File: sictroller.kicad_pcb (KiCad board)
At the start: 6 copper layers, 314 parts, among them J1 CONN_01X02, J10 CONN_01X02, J11 RINGTERM, J12 RINGTERM, J13 CONN_01X01, J2 CONN_01X08, J3 CONN_02X05, J4 RINGTERM, J5 RINGTERM, J6 RINGTERM, J7 CONN_01X02, J8 RINGTERM, J9 RINGTERM, P1 CONN_01X03, Q1 CSD17483F4, Q2 CCS050M12CM2, T1 7508110151, U1 ACPL-M61L, U10 74LVC2G04, U11 TXS0108E, U12 MGJ1, U13 MGJ1, U14 2ED020I12-F2, U15 MGJ1, U16 MGJ1, U17 2ED020I12-F2, U18 MGJ1, U19 MGJ1, U2 TMS320F28069M, U20 2ED020I12-F2, U3 ADM3053, U4 TPS76201, U5 TPS76201, U6 XCL221B18, U7 VIPER26HD, U8 ADUM5241, U9 MAX6691, Y1 CSTCE20M0V13C

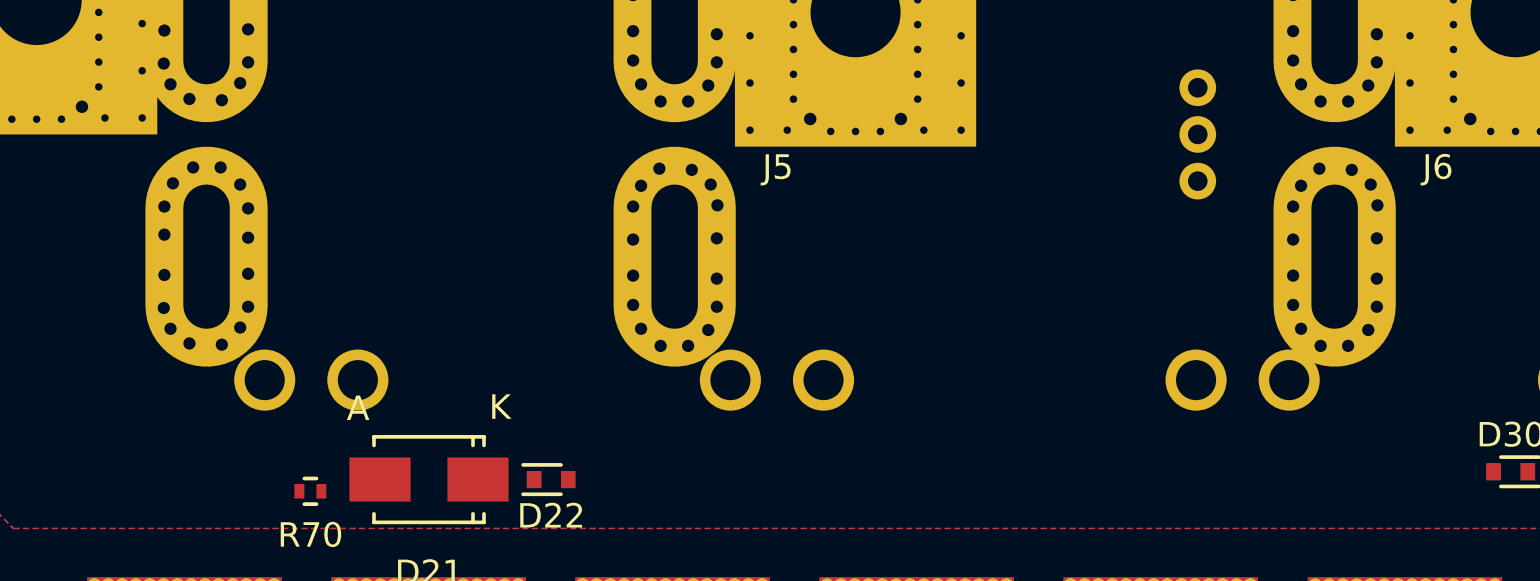
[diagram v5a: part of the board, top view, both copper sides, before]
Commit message: Zones for phase connections
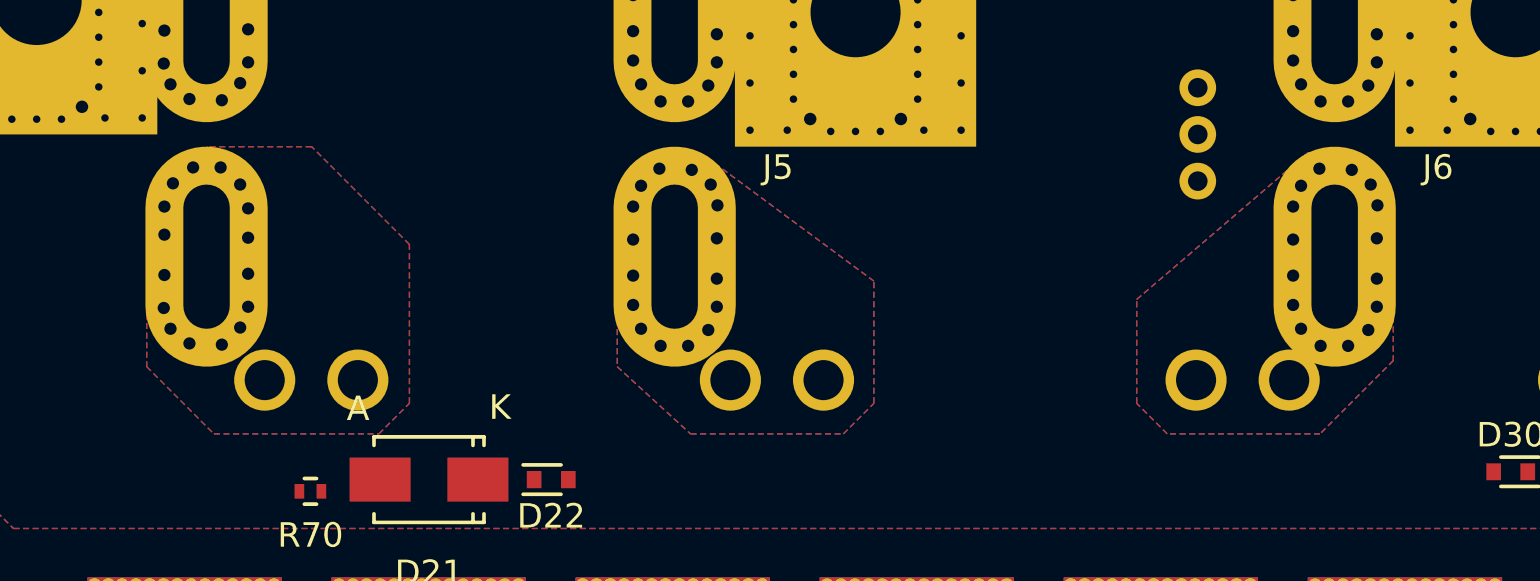
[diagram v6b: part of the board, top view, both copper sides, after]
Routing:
- added copper zone on B.Cu, net PHASE_A
- added copper zone on F.Cu, net PHASE_A
- added copper zone on In1.Cu, net PHASE_A
- added copper zone on In2.Cu, net PHASE_A
- added copper zone on In3.Cu, net PHASE_A
- added copper zone on In4.Cu, net PHASE_A
- added copper zone on B.Cu, net PHASE_B
- added copper zone on F.Cu, net PHASE_B
- added copper zone on In1.Cu, net PHASE_B
- added copper zone on In2.Cu, net PHASE_B
- added copper zone on In3.Cu, net PHASE_B
- added copper zone on In4.Cu, net PHASE_B
- added copper zone on B.Cu, net PHASE_C
- added copper zone on F.Cu, net PHASE_C
- added copper zone on In1.Cu, net PHASE_C
- added copper zone on In2.Cu, net PHASE_C
- added copper zone on In3.Cu, net PHASE_C
- added copper zone on In4.Cu, net PHASE_C
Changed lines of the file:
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@@
 (kicad_pcb (version 4) (host pcbnew 4.0.4+dfsg1-stable)
   (general
-    (links 0)
-    (no_connects 664)
+    (links 2688)
+    (no_connects 658)
     (area 0 0 0 0)
     (thickness 2.36)
@@
   (layers
     (0 F.Cu signal)
-    (1 In1.Cu mixed hide)
-    (2 In2.Cu mixed hide)
-    (3 In3.Cu mixed hide)
-    (4 In4.Cu mixed hide)
+    (1 In1.Cu mixed)
+    (2 In2.Cu mixed)
+    (3 In3.Cu mixed)
+    (4 In4.Cu mixed)
     (31 B.Cu signal)
     (32 B.Adhes user hide)
@@
     (trace_clearance 0.177)
     (zone_clearance 0.4)
-    (zone_45_only yes)
+    (zone_45_only no)
     (trace_min 0.177)
     (segment_width 0.2)
@@
       )
     )
+  )
+  (zone (net 58) (net_name PHASE_A) (layer F.Cu) (hatch edge 0.508)
+    (connect_pads yes (clearance 0.8))
+    (min_thickness 0.2032)
+    (fill yes (arc_segments 32) (thermal_gap 0.508) (thermal_bridge_width 0.508))
+    (polygon
+      (pts
+        (xy 84.5 51.25) (xy 85.75 50) (xy 85.75 43.5) (xy 81.75 39.5) (xy 77.5 39.5)
+        (xy 75 42) (xy 75 48.5) (xy 77.75 51.25)
+      )
+    )
+  )
+  (zone (net 65) (net_name PHASE_B) (layer F.Cu) (hatch edge 0.508)
+    (connect_pads yes (clearance 0.8))
+    (min_thickness 0.2032)
+    (fill yes (arc_segments 32) (thermal_gap 0.508) (thermal_bridge_width 0.508))
+    (polygon
+      (pts
+        (xy 103.5 51.25) (xy 104.75 50) (xy 104.75 45) (xy 98 40) (xy 95.25 40)
+        (xy 94.25 42.25) (xy 94.25 48.5) (xy 97.25 51.25)
+      )
+    )
+  )
+  (zone (net 72) (net_name PHASE_C) (layer F.Cu) (hatch edge 0.508)
+    (connect_pads yes (clearance 0.8))
+    (min_thickness 0.2032)
+    (fill yes (arc_segments 32) (thermal_gap 0.508) (thermal_bridge_width 0.508))
+    (polygon
+      (pts
+        (xy 116.75 51.25) (xy 115.5 50) (xy 115.5 45.75) (xy 122.5 39.75) (xy 124.5 39.75)
+        (xy 126 41.75) (xy 126 48.25) (xy 123 51.25)
+      )
+    )
+  )
+  (zone (net 58) (net_name PHASE_A) (layer B.Cu) (hatch edge 0.508)
+    (connect_pads yes (clearance 0.8))
+    (min_thickness 0.2032)
+    (fill yes (arc_segments 32) (thermal_gap 0.508) (thermal_bridge_width 0.508))
+    (polygon
+      (pts
+        (xy 84.5 51.25) (xy 85.75 50) (xy 85.75 43.5) (xy 81.75 39.5) (xy 77.5 39.5)
+        (xy 75 42) (xy 75 48.5) (xy 77.75 51.25)
+      )
+    )
+  )
+  (zone (net 58) (net_name PHASE_A) (layer In1.Cu) (hatch edge 0.508)
+    (connect_pads yes (clearance 0.4))
+    (min_thickness 0.2032)
+    (fill yes (arc_segments 32) (thermal_gap 0.508) (thermal_bridge_width 0.508))
+    (polygon
+      (pts
+        (xy 84.5 51.25) (xy 85.75 50) (xy 85.75 43.5) (xy 81.75 39.5) (xy 77.5 39.5)
+        (xy 75 42) (xy 75 48.5) (xy 77.75 51.25)
+      )
+    )
+  )
+  (zone (net 58) (net_name PHASE_A) (layer In2.Cu) (hatch edge 0.508)
+    (connect_pads yes (clearance 0.4))
+    (min_thickness 0.2032)
+    (fill yes (arc_segments 32) (thermal_gap 0.508) (thermal_bridge_width 0.508))
+    (polygon
+      (pts
+        (xy 84.5 51.25) (xy 85.75 50) (xy 85.75 43.5) (xy 81.75 39.5) (xy 77.5 39.5)
+        (xy 75 42) (xy 75 48.5) (xy 77.75 51.25)
+      )
+    )
+  )
+  (zone (net 58) (net_name PHASE_A) (layer In3.Cu) (hatch edge 0.508)
+    (connect_pads yes (clearance 0.4))
+    (min_thickness 0.2032)
+    (fill yes (arc_segments 32) (thermal_gap 0.508) (thermal_bridge_width 0.508))
+    (polygon
+      (pts
+        (xy 84.5 51.25) (xy 85.75 50) (xy 85.75 43.5) (xy 81.75 39.5) (xy 77.5 39.5)
+        (xy 75 42) (xy 75 48.5) (xy 77.75 51.25)
+      )
+    )
+  )
+  (zone (net 58) (net_name PHASE_A) (layer In4.Cu) (hatch edge 0.508)
+    (connect_pads yes (clearance 0.4))
+    (min_thickness 0.2032)
+    (fill yes (arc_segments 32) (thermal_gap 0.508) (thermal_bridge_width 0.508))
+    (polygon
+      (pts
+        (xy 84.5 51.25) (xy 85.75 50) (xy 85.75 43.5) (xy 81.75 39.5) (xy 77.5 39.5)
+        (xy 75 42) (xy 75 48.5) (xy 77.75 51.25)
+      )
+    )
+  )
+  (zone (net 65) (net_name PHASE_B) (layer B.Cu) (hatch edge 0.508)
+    (connect_pads yes (clearance 0.8))
+    (min_thickness 0.2032)
+    (fill yes (arc_segments 32) (thermal_gap 0.508) (thermal_bridge_width 0.508))
+    (polygon
+      (pts
+        (xy 103.5 51.25) (xy 104.75 50) (xy 104.75 45) (xy 98 40) (xy 95.25 40)
+        (xy 94.25 42.25) (xy 94.25 48.5) (xy 97.25 51.25)
+      )
+    )
+  )
+  (zone (net 65) (net_name PHASE_B) (layer In1.Cu) (hatch edge 0.508)
+    (connect_pads yes (clearance 0.4))
+    (min_thickness 0.2032)
+    (fill yes (arc_segments 32) (thermal_gap 0.508) (thermal_bridge_width 0.508))
+    (polygon
+      (pts
+        (xy 103.5 51.25) (xy 104.75 50) (xy 104.75 45) (xy 98 40) (xy 95.25 40)
+        (xy 94.25 42.25) (xy 94.25 48.5) (xy 97.25 51.25)
+      )
+    )
+  )
+  (zone (net 65) (net_name PHASE_B) (layer In2.Cu) (hatch edge 0.508)
+    (connect_pads yes (clearance 0.4))
+    (min_thickness 0.2032)
+    (fill yes (arc_segments 32) (thermal_gap 0.508) (thermal_bridge_width 0.508))
+    (polygon
+      (pts
+        (xy 103.5 51.25) (xy 104.75 50) (xy 104.75 45) (xy 98 40) (xy 95.25 40)
+        (xy 94.25 42.25) (xy 94.25 48.5) (xy 97.25 51.25)
+      )
+    )
+  )
+  (zone (net 65) (net_name PHASE_B) (layer In3.Cu) (hatch edge 0.508)
+    (connect_pads yes (clearance 0.4))
+    (min_thickness 0.2032)
+    (fill yes (arc_segments 32) (thermal_gap 0.508) (thermal_bridge_width 0.508))
+    (polygon
+      (pts
+        (xy 103.5 51.25) (xy 104.75 50) (xy 104.75 45) (xy 98 40) (xy 95.25 40)
+        (xy 94.25 42.25) (xy 94.25 48.5) (xy 97.25 51.25)
+      )
+    )
+  )
+  (zone (net 65) (net_name PHASE_B) (layer In4.Cu) (hatch edge 0.508)
+    (connect_pads yes (clearance 0.4))
+    (min_thickness 0.2032)
+    (fill yes (arc_segments 32) (thermal_gap 0.508) (thermal_bridge_width 0.508))
+    (polygon
+      (pts
+        (xy 103.5 51.25) (xy 104.75 50) (xy 104.75 45) (xy 98 40) (xy 95.25 40)
+        (xy 94.25 42.25) (xy 94.25 48.5) (xy 97.25 51.25)
+      )
+    )
+  )
+  (zone (net 72) (net_name PHASE_C) (layer B.Cu) (hatch edge 0.508)
+    (connect_pads yes (clearance 0.8))
+    (min_thickness 0.2032)
+    (fill yes (arc_segments 32) (thermal_gap 0.508) (thermal_bridge_width 0.508))
+    (polygon
+      (pts
+        (xy 116.75 51.25) (xy 115.5 50) (xy 115.5 45.75) (xy 122.5 39.75) (xy 124.5 39.75)
+        (xy 126 41.75) (xy 126 48.25) (xy 123 51.25)
+      )
+    )
+  )
+  (zone (net 72) (net_name PHASE_C) (layer In1.Cu) (hatch edge 0.508)
+    (connect_pads yes (clearance 0.4))
+    (min_thickness 0.2032)
+    (fill yes (arc_segments 32) (thermal_gap 0.508) (thermal_bridge_width 0.508))
+    (polygon
+      (pts
+        (xy 116.75 51.25) (xy 115.5 50) (xy 115.5 45.75) (xy 122.5 39.75) (xy 124.5 39.75)
+        (xy 126 41.75) (xy 126 48.25) (xy 123 51.25)
+      )
+    )
+  )
+  (zone (net 72) (net_name PHASE_C) (layer In2.Cu) (hatch edge 0.508)
+    (connect_pads yes (clearance 0.4))
+    (min_thickness 0.2032)
+    (fill yes (arc_segments 32) (thermal_gap 0.508) (thermal_bridge_width 0.508))
+    (polygon
+      (pts
+        (xy 116.75 51.25) (xy 115.5 50) (xy 115.5 45.75) (xy 122.5 39.75) (xy 124.5 39.75)
+        (xy 126 41.75) (xy 126 48.25) (xy 123 51.25)
+      )
+    )
+  )
+  (zone (net 72) (net_name PHASE_C) (layer In3.Cu) (hatch edge 0.508)
+    (connect_pads yes (clearance 0.4))
+    (min_thickness 0.2032)
+    (fill yes (arc_segments 32) (thermal_gap 0.508) (thermal_bridge_width 0.508))
+    (polygon
+      (pts
+        (xy 116.75 51.25) (xy 115.5 50) (xy 115.5 45.75) (xy 122.5 39.75) (xy 124.5 39.75)
+        (xy 126 41.75) (xy 126 48.25) (xy 123 51.25)
+      )
+    )
+  )
+  (zone (net 72) (net_name PHASE_C) (layer In4.Cu) (hatch edge 0.508)
+    (connect_pads yes (clearance 0.4))
+    (min_thickness 0.2032)
+    (fill yes (arc_segments 32) (thermal_gap 0.508) (thermal_bridge_width 0.508))
+    (polygon
+      (pts
+        (xy 116.75 51.25) (xy 115.5 50) (xy 115.5 45.75) (xy 122.5 39.75) (xy 124.5 39.75)
+        (xy 126 41.75) (xy 126 48.25) (xy 123 51.25)
+      )
+    )

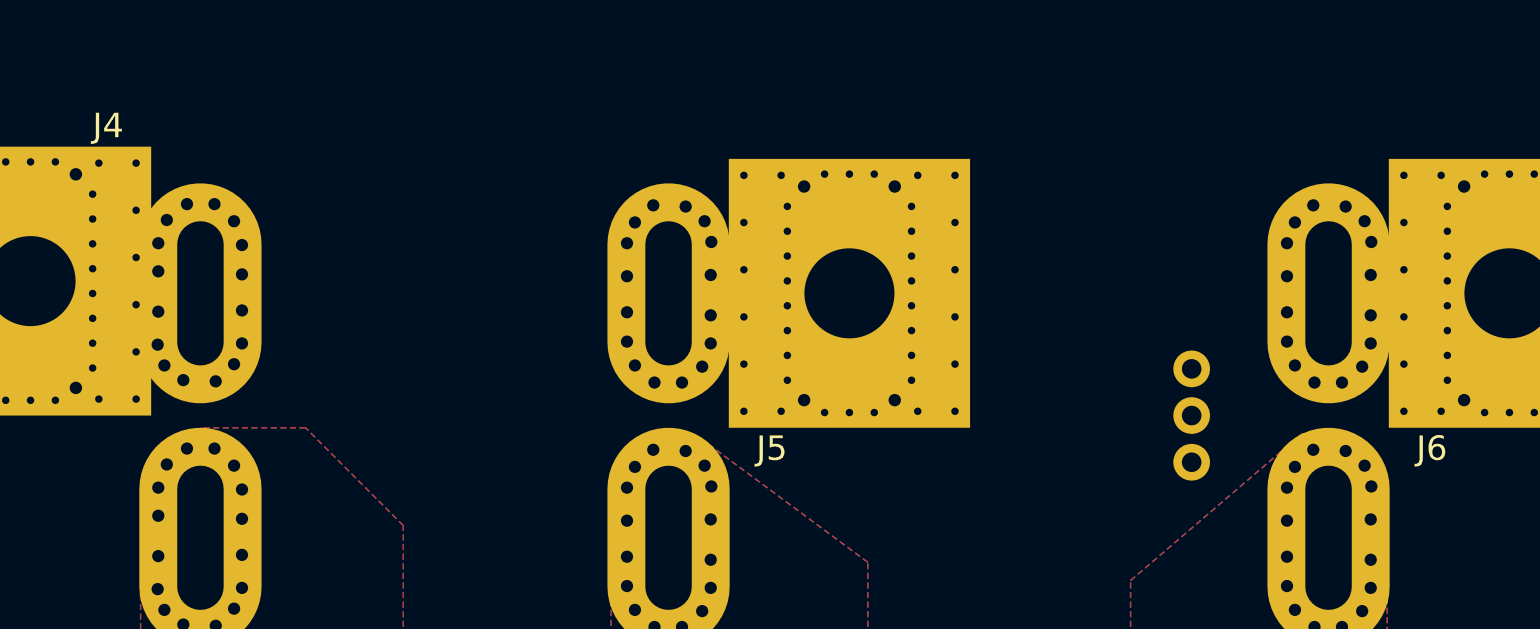
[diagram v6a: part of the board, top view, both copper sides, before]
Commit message: Zones for phase connections 2
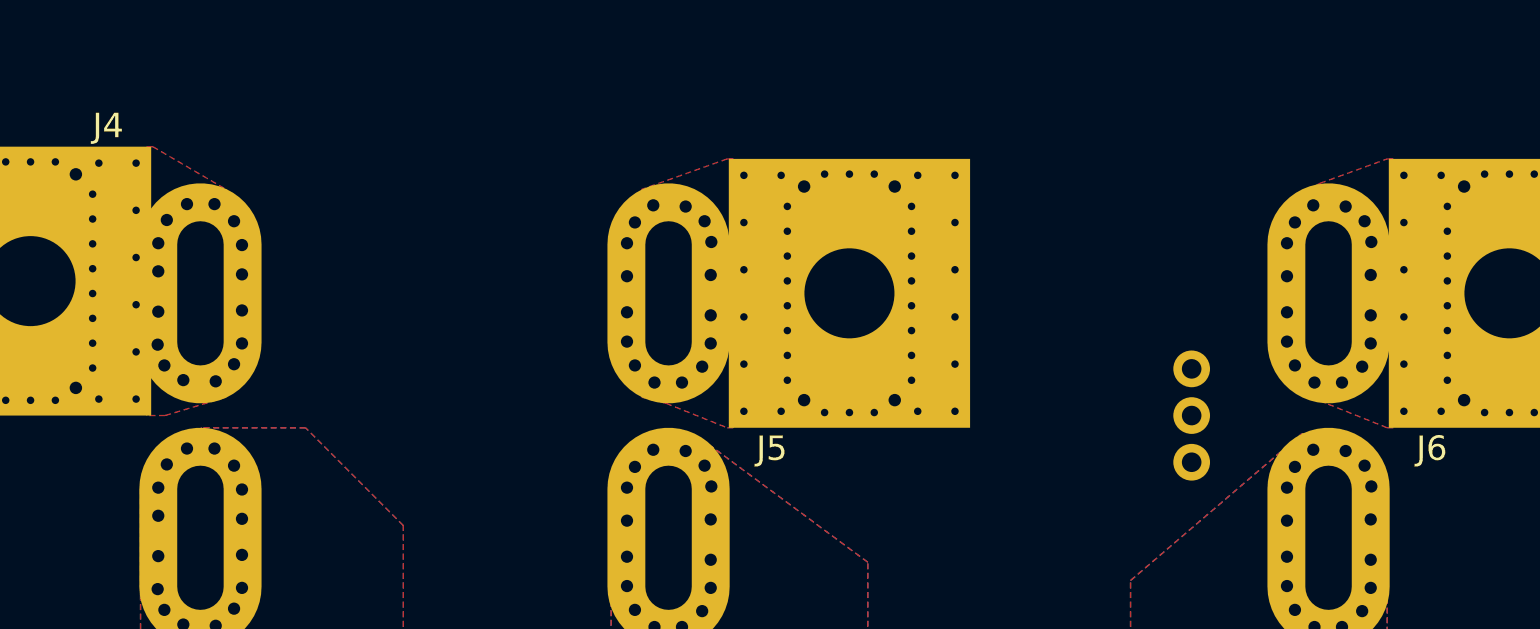
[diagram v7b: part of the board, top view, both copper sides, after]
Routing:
- added copper zone on F.Cu, net /Feedback/A
- added copper zone on F.Cu, net /Feedback/B
- added copper zone on F.Cu, net /Feedback/C
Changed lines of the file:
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@@
     (links 2688)
     (no_connects 658)
-    (area 0 0 0 0)
+    (area 13.356 -160.267 249.056667 133.600001)
     (thickness 2.36)
     (drawings 8)
@@
     (user_trace_width 9.144)
     (trace_clearance 0.177)
-    (zone_clearance 0.4)
+    (zone_clearance 0.65)
     (zone_45_only no)
     (trace_min 0.177)
@@
     (visible_elements FFFCF77F)
     (pcbplotparams
-      (layerselection 0x010f8_ffffffff)
+      (layerselection 0x010f8_8000001f)
       (usegerberextensions true)
       (excludeedgelayer true)
@@
     (polygon
       (pts
-        (xy 116.75 51.25) (xy 115.5 50) (xy 115.5 45.75) (xy 122.5 39.75) (xy 124.5 39.75)
+        (xy 116.75 51.25) (xy 115.5 50) (xy 115.5 45.75) (xy 122.5 39.75) (xy 124.25 39.75)
         (xy 126 41.75) (xy 126 48.25) (xy 123 51.25)
       )
@@
     (polygon
       (pts
-        (xy 116.75 51.25) (xy 115.5 50) (xy 115.5 45.75) (xy 122.5 39.75) (xy 124.5 39.75)
+        (xy 116.75 51.25) (xy 115.5 50) (xy 115.5 45.75) (xy 122.5 39.75) (xy 124.25 39.75)
         (xy 126 41.75) (xy 126 48.25) (xy 123 51.25)
       )
@@
     (polygon
       (pts
-        (xy 116.75 51.25) (xy 115.5 50) (xy 115.5 45.75) (xy 122.5 39.75) (xy 124.5 39.75)
+        (xy 116.75 51.25) (xy 115.5 50) (xy 115.5 45.75) (xy 122.5 39.75) (xy 124.25 39.75)
         (xy 126 41.75) (xy 126 48.25) (xy 123 51.25)
       )
@@
     (polygon
       (pts
-        (xy 116.75 51.25) (xy 115.5 50) (xy 115.5 45.75) (xy 122.5 39.75) (xy 124.5 39.75)
+        (xy 116.75 51.25) (xy 115.5 50) (xy 115.5 45.75) (xy 122.5 39.75) (xy 124.25 39.75)
         (xy 126 41.75) (xy 126 48.25) (xy 123 51.25)
       )
@@
     (polygon
       (pts
-        (xy 116.75 51.25) (xy 115.5 50) (xy 115.5 45.75) (xy 122.5 39.75) (xy 124.5 39.75)
+        (xy 116.75 51.25) (xy 115.5 50) (xy 115.5 45.75) (xy 122.5 39.75) (xy 124.25 39.75)
         (xy 126 41.75) (xy 126 48.25) (xy 123 51.25)
       )
@@
     (polygon
       (pts
-        (xy 116.75 51.25) (xy 115.5 50) (xy 115.5 45.75) (xy 122.5 39.75) (xy 124.5 39.75)
+        (xy 116.75 51.25) (xy 115.5 50) (xy 115.5 45.75) (xy 122.5 39.75) (xy 124.25 39.75)
         (xy 126 41.75) (xy 126 48.25) (xy 123 51.25)
       )
     )
+  )
+  (zone (net 140) (net_name /Feedback/A) (layer F.Cu) (hatch edge 0.508)
+    (connect_pads yes (clearance 0.65))
+    (min_thickness 0.2032)
+    (fill yes (arc_segments 32) (thermal_gap 0.508) (thermal_bridge_width 0.508))
+    (polygon
+      (pts
+        (xy 75.5 28) (xy 78.5 29.75) (xy 78.5 38.25) (xy 76 39) (xy 75.25 39)
+        (xy 75.25 28)
+      )
+    )
+  )
+  (zone (net 141) (net_name /Feedback/B) (layer F.Cu) (hatch edge 0.508)
+    (connect_pads yes (clearance 0.65))
+    (min_thickness 0.2032)
+    (fill yes (arc_segments 32) (thermal_gap 0.508) (thermal_bridge_width 0.508))
+    (polygon
+      (pts
+        (xy 99.25 28.5) (xy 99 28.5) (xy 95.5 29.75) (xy 95.5 38.25) (xy 96.5 38.5)
+        (xy 99 39.5) (xy 99.25 39.5)
+      )
+    )
+  )
+  (zone (net 142) (net_name /Feedback/C) (layer F.Cu) (hatch edge 0.508)
+    (connect_pads yes (clearance 0.6))
+    (min_thickness 0.2032)
+    (fill yes (arc_segments 32) (thermal_gap 0.508) (thermal_bridge_width 0.508))
+    (polygon
+      (pts
+        (xy 123.5 38.5) (xy 122.75 38) (xy 122.75 29.75) (xy 123.25 29.5) (xy 126 28.5)
+        (xy 126.25 28.5) (xy 126.25 39.5) (xy 126 39.5)
+      )
+    )
